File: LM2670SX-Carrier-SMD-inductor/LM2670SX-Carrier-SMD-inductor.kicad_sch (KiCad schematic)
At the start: 10 parts, among them IC1 LM2670SX-3.3_NOPB, J1 Conn_01x03

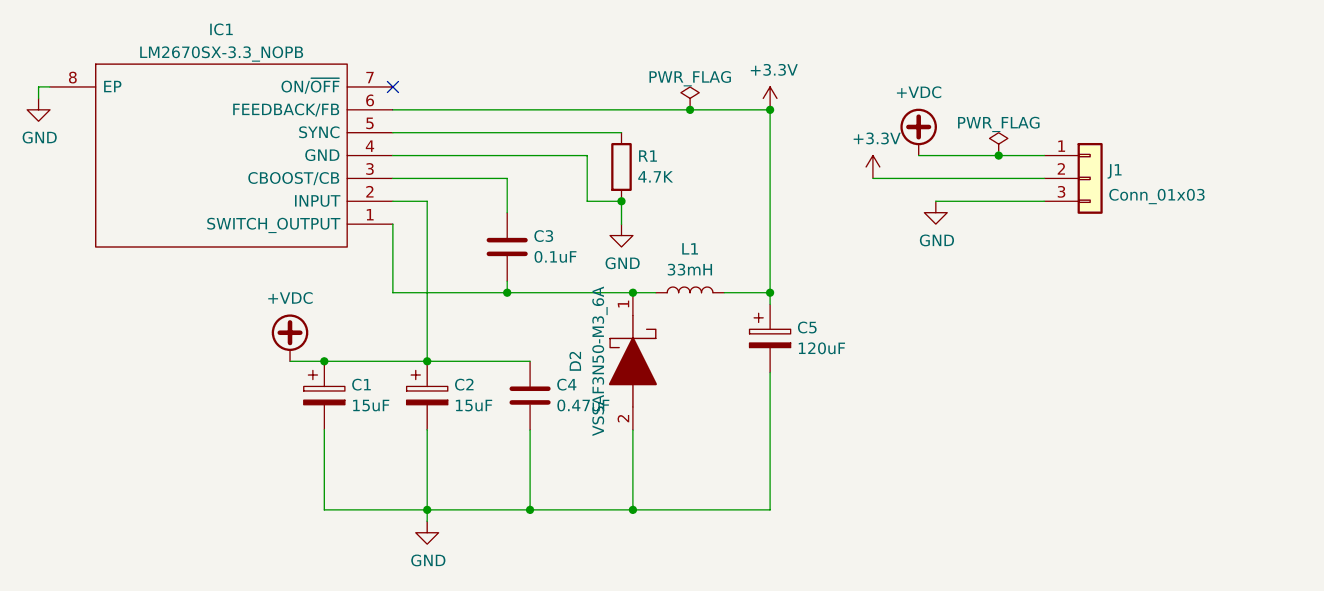
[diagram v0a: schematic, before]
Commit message: adding fab files for Fixed SMD inductror adding that as well. sent off to fab
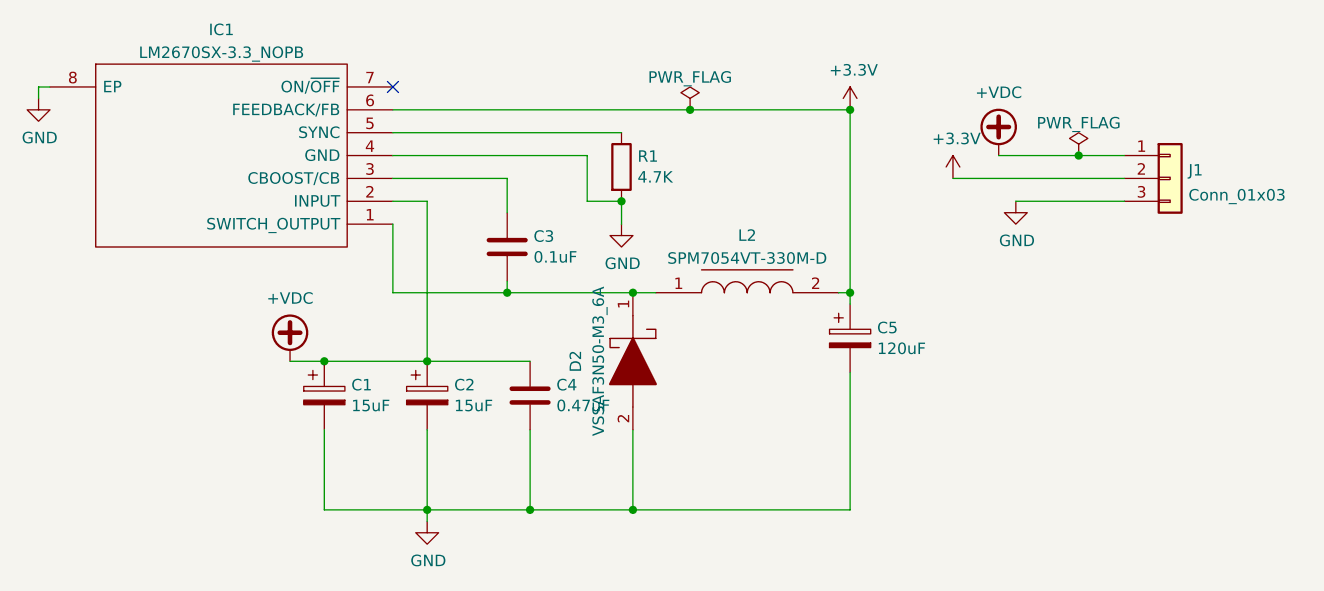
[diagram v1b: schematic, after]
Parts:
- removed L1: 33mH, Inductor_THT:L_Axial_L9.5mm_D4.0mm_P15.24mm_Horizontal_Fastron_SMCC, symbol Device:L
- added L2: SPM7054VT-330M-D, SPM7054VT, symbol SamacSys_Parts:SPM7054VT-330M-D
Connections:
- net +3V3: now also L2.2
- net at C3.2, D2.1, IC1.1 (SWITCH_OUTPUT): now also L2.1
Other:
- moved on the sheet: C5, J1

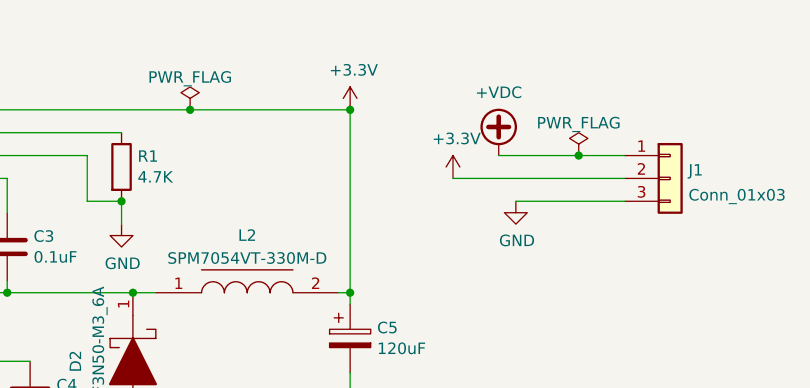
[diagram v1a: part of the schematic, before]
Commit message: clean up p2
removed pcb zips
upgraded projects to kicad 8
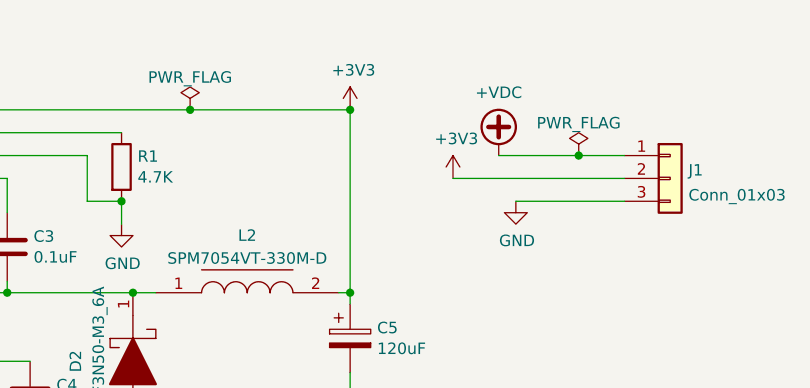
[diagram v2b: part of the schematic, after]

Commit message: update footprints in schematic only
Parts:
- C3, C4: footprint Capacitor_SMD:C_0603_1608Metric_Pad1.08x0.95mm_HandSolder -> Capacitor_SMD:C_1206_3216Metric_Pad1.33x1.80mm_HandSolder
- R1: footprint Resistor_SMD:R_0612_1632Metric_Pad1.18x3.40mm_HandSolder -> Capacitor_SMD:C_1206_3216Metric_Pad1.33x1.80mm_HandSolder
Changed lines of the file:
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@@
 			)
 		)
-		(property "Footprint" "Capacitor_SMD:C_0603_1608Metric_Pad1.08x0.95mm_HandSolder"
+		(property "Footprint" "Capacitor_SMD:C_1206_3216Metric_Pad1.33x1.80mm_HandSolder"
 			(at 144.4752 95.25 0)
 			(effects
@@
 			)
 		)
-		(property "Footprint" "Capacitor_SMD:C_0603_1608Metric_Pad1.08x0.95mm_HandSolder"
+		(property "Footprint" "Capacitor_SMD:C_1206_3216Metric_Pad1.33x1.80mm_HandSolder"
 			(at 147.0152 111.76 0)
 			(effects
@@
 			)
 		)
-		(property "Footprint" "Resistor_SMD:R_0612_1632Metric_Pad1.18x3.40mm_HandSolder"
+		(property "Footprint" "Capacitor_SMD:C_1206_3216Metric_Pad1.33x1.80mm_HandSolder"
 			(at 154.432 82.55 90)
 			(effects
